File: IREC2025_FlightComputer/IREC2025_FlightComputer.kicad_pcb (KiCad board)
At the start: 4 copper layers, 63.6 x 117.5 mm, 144 parts, among them J1 Molex Microfit, J2 BOOT0, J3 Companion, J5 SWD, Q1 SI7232DN-T1-GE3, U1 STM32U575VGTx, U10 PE4259-63, U11 SX1262IMLTRT, U12 ADXL375BCCZ-RL7, U13 MMC5983MA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

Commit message: small fixes
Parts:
- added LED3: HS-0402-UR, EasyEDA:LED0402-R-RD, F.Cu at (119.7, 106.0)
- added R39: 1kΩ, PCM_JLCPCB:R_0402, F.Cu at (120.2, 103.7)
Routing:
- net Net-(LED3--): track 0.00 -> 1.68 mm
- net +3.3V: track 67.6 -> 68.8 mm, vias 40 -> 41
- net VBAT-: vias 252 -> 253
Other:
- board text added: "PWR"

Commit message: Minor changes
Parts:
- moved LED1 3.89 mm to (89.6, 77.5)
- moved R35 3.89 mm to (89.4, 76.0)
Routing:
- net VBAT-: track 95.5 -> 116.2 mm, vias 253 -> 266
- net +5V: track 56.2 -> 58.8 mm
- net PPS: track 27.7 -> 25.9 mm

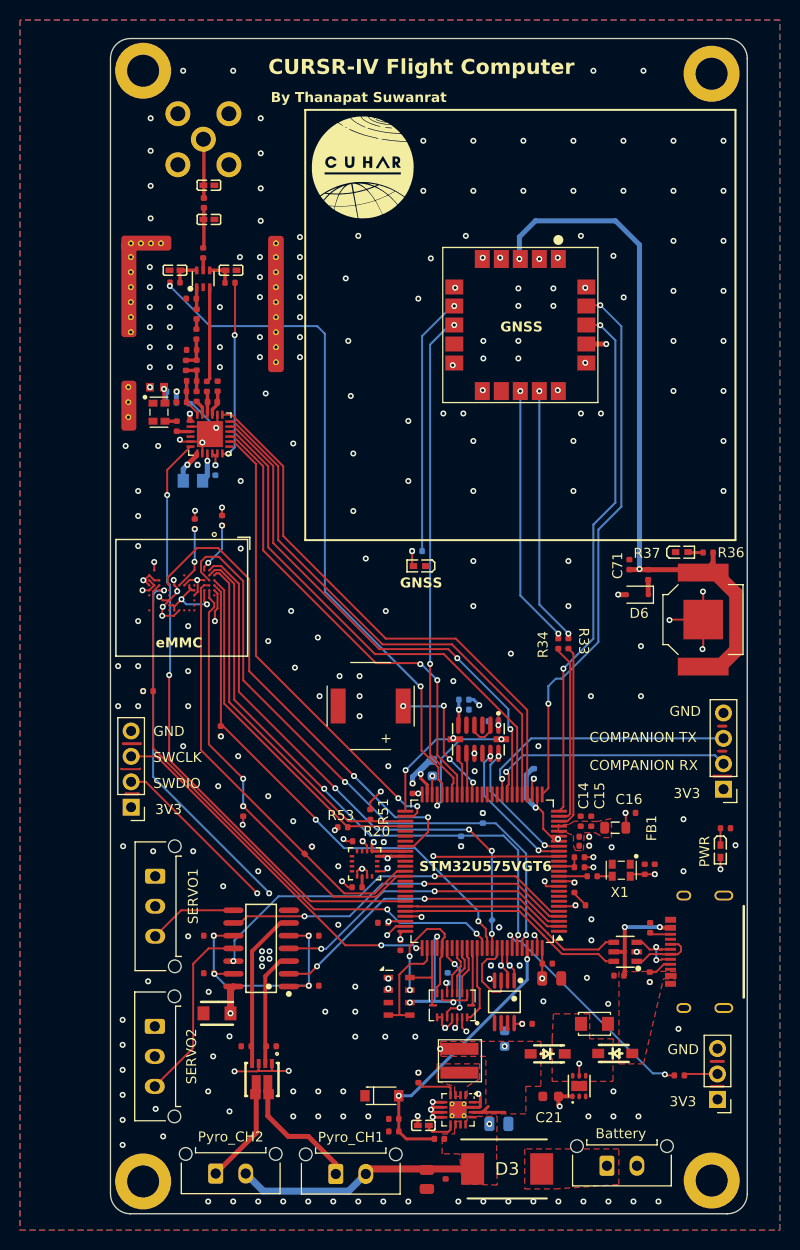
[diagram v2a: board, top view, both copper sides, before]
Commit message: Added silkscreen + Layout Minorchange
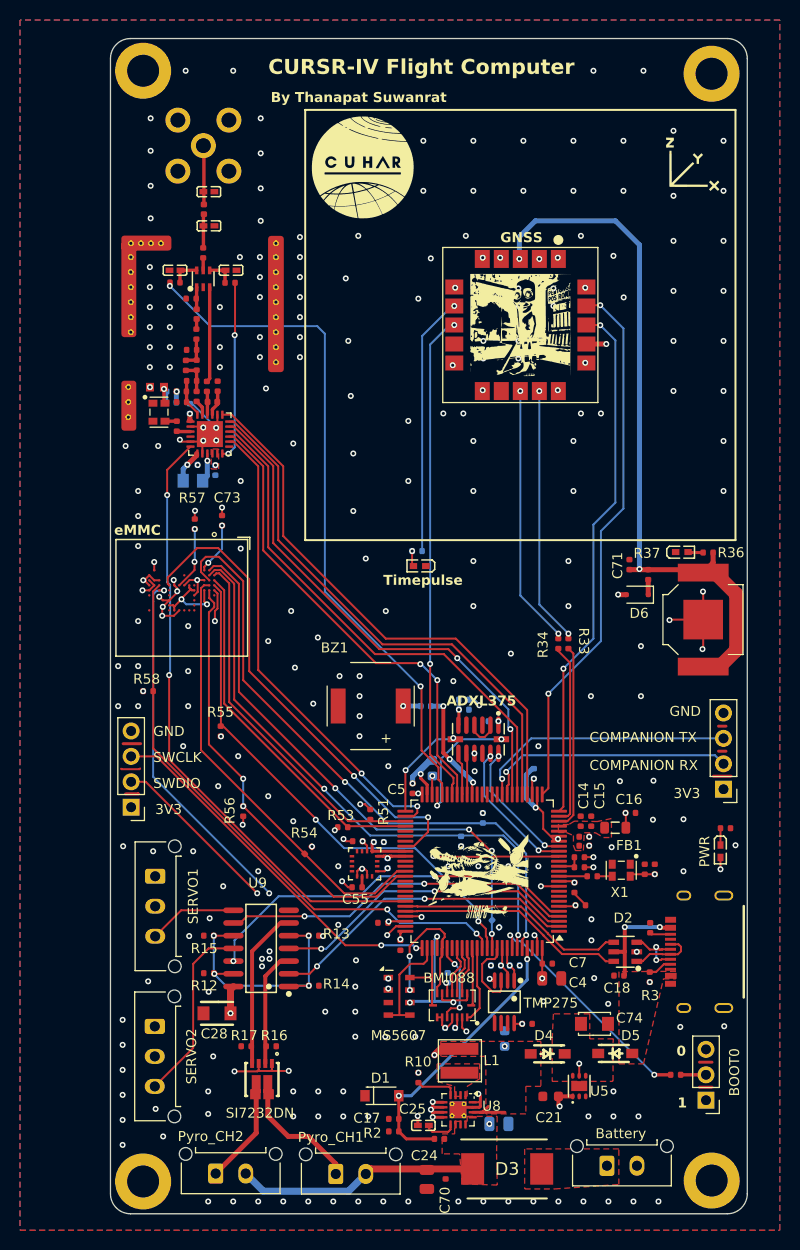
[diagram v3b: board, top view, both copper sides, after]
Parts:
- added G***: LOGO, LOGO, F.Cu at (117.0, 37.8)
- added G***: LOGO, LOGO, F.Cu at (95.5, 108.1)
- added G***: LOGO, LOGO, F.Cu at (99.7, 53.4)
- added R5: 470Ω, PCM_JLCPCB:R_0402, B.Cu at (90.2, 91.5)
- moved J2 1.15 mm to (118.2, 130.9)
- moved C46 0.64 mm to (68.6, 43.5)
- moved C47 0.64 mm to (68.6, 40.1)
- moved RF1 0.64 mm to (68.0, 35.5)
- moved L9 0.64 mm to (68.1, 41.8)
- moved R9 0.37 mm to (115.2, 128.3)
- renumbered U2 to D4, U4 to D5
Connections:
- BZ1 pad 1: BUZZER -> Net-(BZ1-+)
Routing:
- net +3.3V: track 68.8 -> 65.8 mm
- net BUZZER: track 14.2 -> 11.4 mm, vias 4 -> 3
- net Net-(BZ1-+): track 0.00 -> 1.78 mm, vias 0 -> 1
- net VBAT-: track 116.2 -> 117.9 mm, vias 266 -> 278
- net BOOT0: track 3.37 -> 2.53 mm
- net BUSY: track 47.1 -> 47.9 mm
- net Net-(C27-Pad2): track 4.04 -> 3.40 mm
- added copper zone on F.Cu, net +3.3V
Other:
- board text added: "0"
- board text added: "1"
- board text added: "ADXL375"
- board text added: "BMI088"
- board text added: "BOOT0"
- board text added: "BZ1"
- board text added: "C11"
- board text added: "C17"
- board text added: "C18"
- board text added: "C20"
- board text added: "C23"
- board text added: "C24"
- board text added: "C25"
- board text added: "C26"
- board text added: "C28"
- board text added: "C4"
- board text added: "C43"
- board text added: "C45"
- board text added: "C5"
- board text added: "C51"
- board text added: "C52"
- board text added: "C53"
- board text added: "C55"
- board text added: "C57"
- board text added: "C58"
- board text added: "C59"
- board text added: "C7"
- board text added: "C70"
- board text added: "C73"
- board text added: "C74"
- board text added: "D1"
- board text added: "D2"
- board text added: "D4"
- board text added: "D5"
- board text added: "L1"
- board text added: "L3"
- board text added: "MS5607"
- board text added: "R10"
- board text added: "R12"
- board text added: "R13"
- board text added: "R14"
- board text added: "R15"
- board text added: "R16"
- board text added: "R17"
- board text added: "R19"
- board text added: "R2"
- board text added: "R21"
- board text added: "R22"
- board text added: "R3"
- board text added: "R35"
- board text added: "R49"
- board text added: "R5"
- board text added: "R50"
- board text added: "R52"
- board text added: "R54"
- board text added: "R55"
- board text added: "R56"
- board text added: "R57"
- board text added: "R58"
- board text added: "SI7232DN"
- board text added: "TMP275"
- board text added: "Timepulse"
- board text added: "U5"
- board text added: "U8"
- board text added: "U9"
- board text removed: "STM32U575VGT6"
